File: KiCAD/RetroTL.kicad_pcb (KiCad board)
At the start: 2 copper layers, 50 x 50 mm, 19 parts, among them J1 Arduino_ProMini_Angeld_Header, P1 MAINS, P2 Leds, P3 Rotary, P4 0-10V, T1 NA03-T2S09/HLK-PM12, U1 G3MB, U2 LM358, U3 LM2596_mod, U4 433Mhz

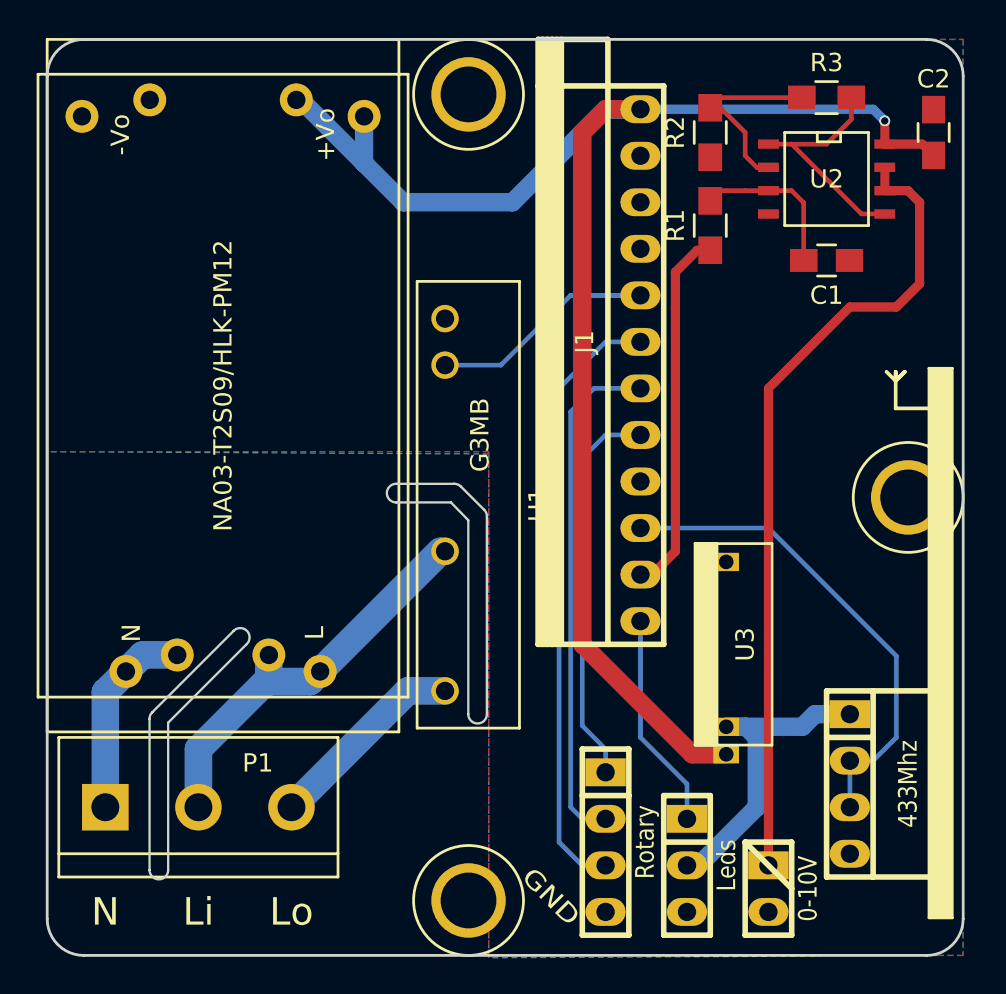
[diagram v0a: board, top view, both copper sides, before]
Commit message: PCB with NRF24N01
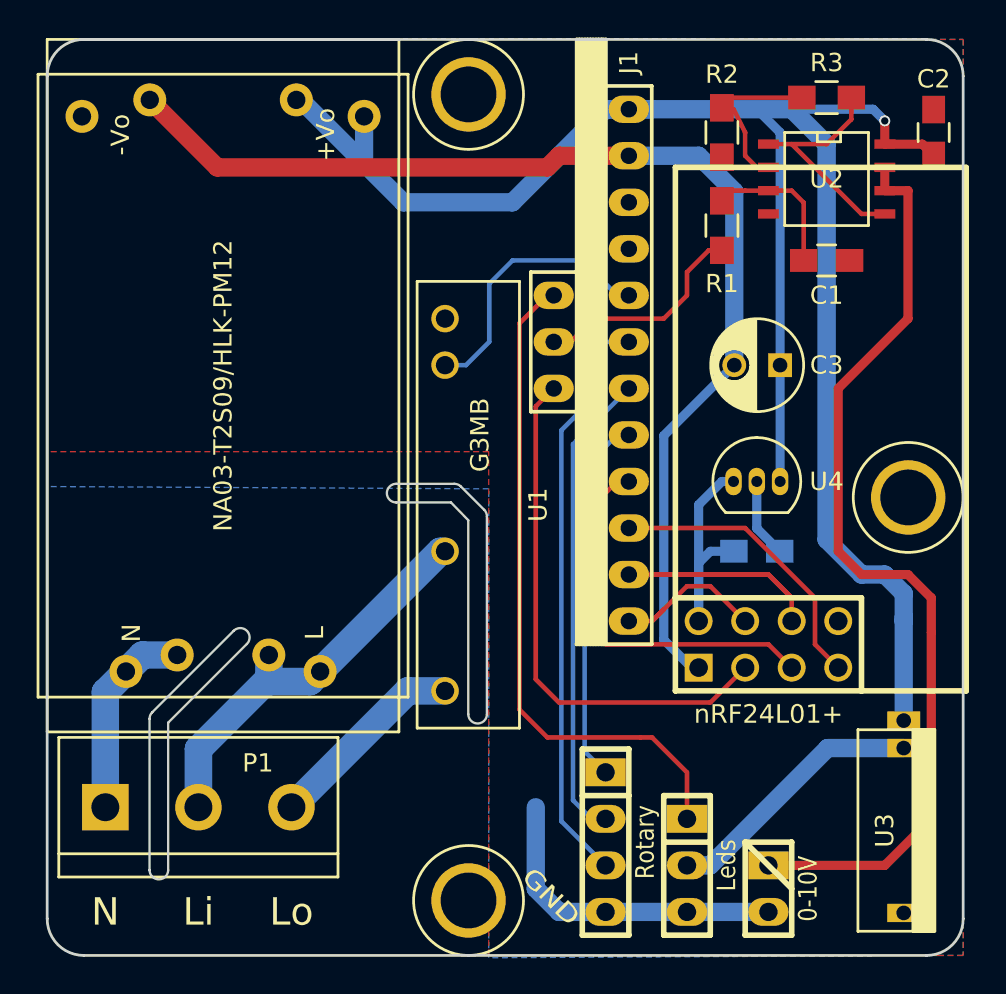
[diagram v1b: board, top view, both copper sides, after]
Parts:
- added C3: CP_Small, Capacitors_ThroughHole:C_Radial_D5_L6_P2.5, F.Cu at (165.0, 95.3)
- added C4: C_Small, Capacitors_SMD:C_0805_HandSoldering, B.Cu at (163.7, 105.4)
- added U5: nRF24L01+, myelin-kicad:NRF24L01_MODULE, F.Cu at (164.4, 110.5)
- J1: footprint septillion_Arduino:arduino_pro_mini_(angle)_header -> septillion_Arduino:Arduino_ProMini_Angeled_Small++
- R1: value 12k -> 100k
- U4: value 433Mhz -> 78L33; footprint septillion_Modules:RM433_receiver_4pin -> TO_SOT_Packages_THT:TO-92_Inline_Narrow_Oval
- moved G*** 31.9 mm to (135.2, 94.0)
- moved U4 17.7 mm to (162.5, 101.6)
- moved U3 13.5 mm to (171.4, 120.7), turned to 270 degrees
- moved R1 0.64 mm to (161.8, 87.7)
- moved R2 0.64 mm to (161.8, 82.6)
- moved J1 0.63 mm to (156.8, 94.0)
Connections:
- J1 pad 13: Net-(J1-Pad13) -> /CSN
- J1 pad 14: Net-(J1-Pad14) -> /MOSI
- J1 pad 15: Net-(J1-Pad15) -> /MISO
- J1 pad 16: Net-(J1-Pad16) -> /SCK
- P2 pad 1: Net-(J1-Pad13) -> Net-(J1-Pad5)
- R1 pad 2: Net-(J1-Pad14) -> Net-(J1-Pad6)
- U4 pad 1: Net-(P2-Pad2) -> +9V
- U4 pad 2: Net-(J1-Pad15) -> GND
- U4 pad 3: Net-(J1-Pad15) -> Net-(C4-Pad1)
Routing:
- net GND: track 0.00 -> 85.1 mm
- net Net-(J1-Pad5): track 0.00 -> 36.7 mm
- net +9V: track 104.2 -> 134.6 mm
- net /CE: track 0.00 -> 29.0 mm
- net Net-(J1-Pad15): track 26.9 -> 0.00 mm
- net /SCK: track 0.00 -> 21.0 mm
- net Net-(J1-Pad14): track 20.1 -> 0.00 mm
- net /MOSI: track 0.00 -> 18.8 mm
- net /MISO: track 0.00 -> 16.1 mm
- net Net-(C4-Pad1): track 0.00 -> 14.2 mm
- net Net-(J1-Pad6): track 0.00 -> 12.0 mm
- net Net-(J1-Pad13): track 11.8 -> 0.00 mm
- net /CSN: track 0.00 -> 8.83 mm
- net Net-(P4-Pad1): track 44.5 -> 51.9 mm
- net Net-(J1-Pad18): track 28.1 -> 26.6 mm
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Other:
- board text added: "RetroTL Dimmer v2 Timo Engelgeer 2016"
- board text removed: "RetroTL Dimmer v1 Timo Engelgeer 2016"

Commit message: Small fixes
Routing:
- net GND: track 85.1 -> 94.0 mm
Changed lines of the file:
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@@
     (thickness 1.6)
     (drawings 44)
-    (tracks 169)
+    (tracks 171)
     (zones 0)
     (modules 22)
@@
   )
   (setup
-    (last_trace_width 1)
+    (last_trace_width 1.5)
     (user_trace_width 0.5)
     (user_trace_width 1)
@@
   )
   (gr_line (start 155.48 125.125) (end 164.37 125.125) (angle 90) (layer F.Mask) (width 1))
-  (gr_text GND (at 153.829 125.633 315) (layer F.SilkS)
+  (gr_text GND (at 153.829 125.633 315) (layer F.Mask)
     (effects (font (size 1 1.2) (thickness 0.2)) (justify right))
   )
@@
   (segment (start 166.295 86.41) (end 165.64 85.755) (width 0.25) (layer F.Cu) (net 1))
   (segment (start 161.83 86.31) (end 161.83 86.263) (width 0.25) (layer F.Cu) (net 1) (status 30))
+  (segment (start 164.37 125.125) (end 159.925 125.125) (width 1.5) (layer F.Cu) (net 2) (status C00000))
+  (segment (start 159.925 125.125) (end 155.48 125.125) (width 1.5) (layer F.Cu) (net 2) (status C00000))
   (segment (start 160.56 111.79) (end 160.179 111.79) (width 0.5) (layer B.Cu) (net 2))
   (segment (start 160.179 111.79) (end 158.655 110.266) (width 0.5) (layer B.Cu) (net 2))
